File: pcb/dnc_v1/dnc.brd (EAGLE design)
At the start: 97.2 x 88 mm, 132 parts, among them IC1 LM2596S, IC2 74S244DW, Q1 IRF9321PBF, Q10 BSS316, Q11 BSS316, Q12 BSS138, Q13 BSS138, Q2 BSS670, Q3 BSS138, Q4 BSS670, Q5 BSS138, Q6 BSS670, Q7 BSS138, Q8 BSS138, Q9 BSS670, U1 MAX202CDWR, U2 74HCT595D, U3 TC7SU04F, U4 AL8807, U5 AL8807, U6 TC7SU04F

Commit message: BOM + carte insa
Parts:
- EXT1: value EXT1 -> EXT
- EXT2: value EXT2 -> EXT
- FLEX: value FLEX -> PLUG-3
- GYRO-LED: value GYRO LED -> PLUG-6
- IC2: value 74S244DW -> 74ACT244SC
- INPUT: value M08 -> PLUG-8
- L2, L3: value 100nH -> 100nH2.4A
- LED10W1: value LED10W1 -> PLUG-2
- LED10W2: value LED10W2 -> PLUG-2
- R12: value (none) -> 5.1K
- RELAY: value RELAY -> PLUG-3
- U4, U5: value AL8807 -> AL8805WS
- renumbered PLUG_3.81_1 to FLEX, PLUG_3.81_2 to RELAY, PLUG_3.81_2_1 to LED10W2, PLUG_3.81_2_2 to LED10W1, PLUG_3.81_6_1 to GYRO-LED, U$6 to INPUT

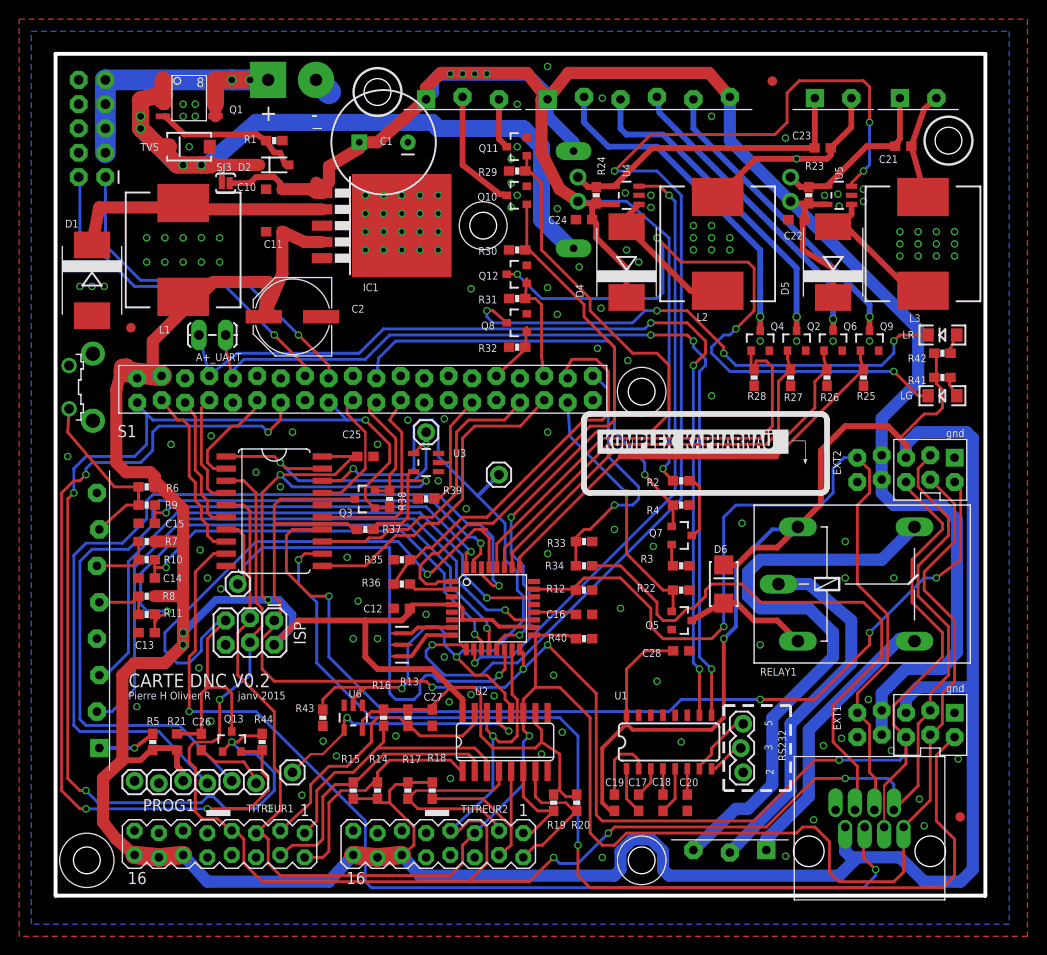
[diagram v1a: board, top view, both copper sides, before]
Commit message: minor debug (hole + value)
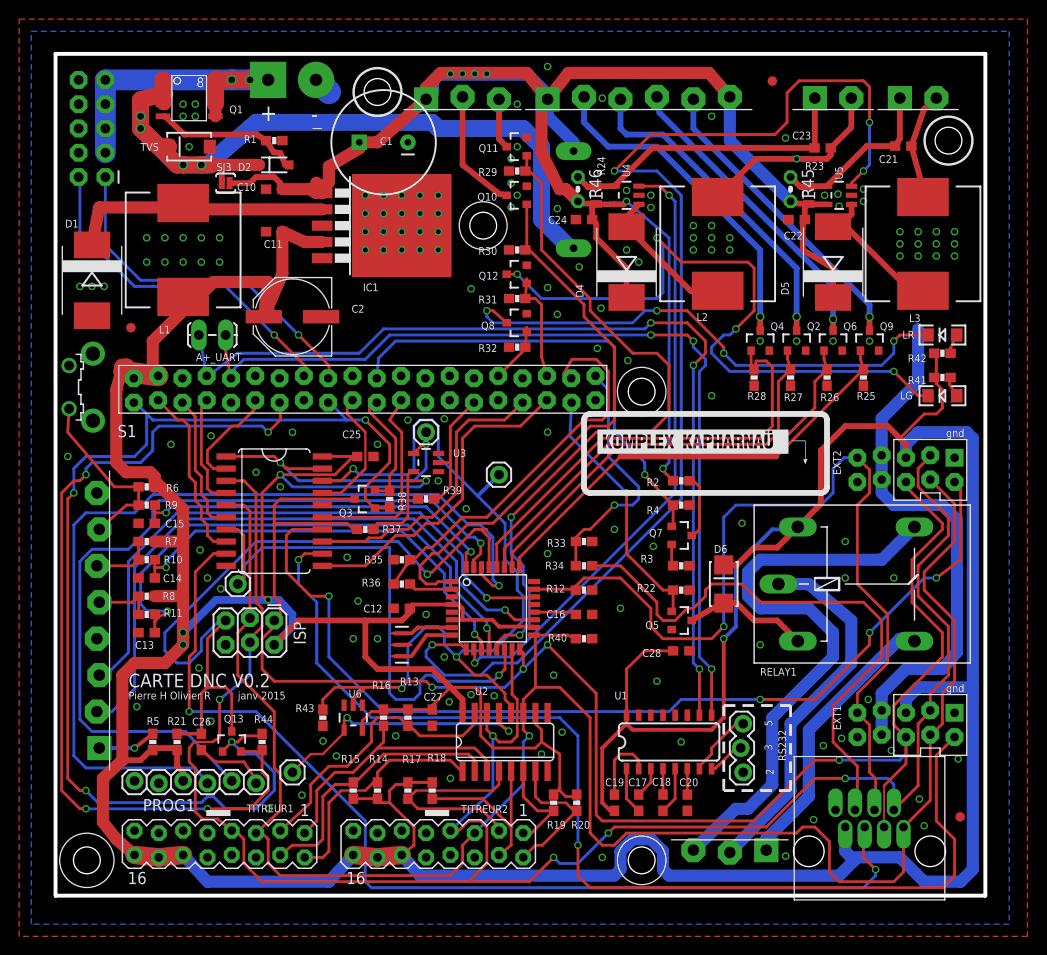
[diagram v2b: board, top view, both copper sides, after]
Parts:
- removed SJ1, SJ2: JUMPER-PTH-2-NO, SparkFun-Passives:PTH-JUMPER-2-NO_NO_SILK
- added R45, R46: OPTIONAL, rcl:0204V
- C1: value 680uF30mm -> 680uF
- R21: device rcl:R0603 -> SparkFun-Passives:0603-RES
- R23, R24: device SparkFun-Passives:0603-RES -> SparkFun-Passives:0805
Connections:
- net LED+1: now also R46.1; no longer SJ1.2
- net LED+2: now also R45.1; no longer SJ2.2
- net RAW_FUSED: now also R45.2, R46.2; no longer SJ1.1, SJ2.1
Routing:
- net RAW_FUSED: track 262.9 -> 240.4 mm, vias 5 -> 6
- net RX-I: track 92.2 -> 94.8 mm
- net +5V: track 568.4 -> 567.2 mm

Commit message: major change correction : - driver led position - add usb for power - correct max 202 voltage problem - titrer connector position - forget line - power trace consideration
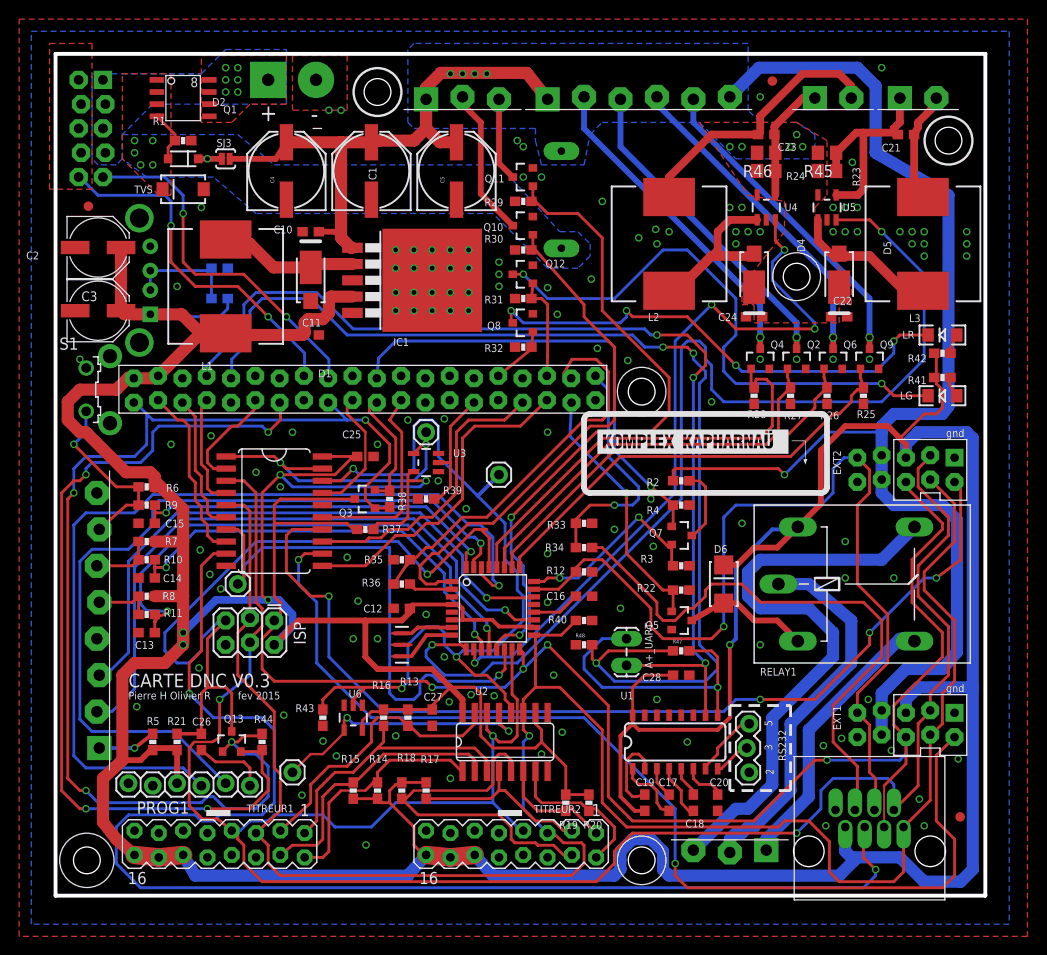
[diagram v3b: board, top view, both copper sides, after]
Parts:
- added C3: 100u, rcl:PANASONIC_D
- added C4, C5: 220uF, SparkFun:PANASONIC_E
- added R47: 10K, SparkFun-Passives:0603-RES
- added R48: 20K, SparkFun-Passives:0603-RES
- added R49: 22K, SparkFun-Passives:0603-RES
- added R50: 33K, SparkFun-Passives:0603-RES
- added X1: USB, pierre_vv:USB_F_SATISTRONIC
- C1: value 680uF -> 220uF; device SparkFun:CPOL-RADIAL-1000UF-25V -> SparkFun:PANASONIC_E
- C2: value 220u -> 100u; device rcl:PANASONIC_E -> rcl:PANASONIC_D
- D1, D4, D5: device diode:SMC -> pierre_vv:DO-221
- JP1: device SparkFun:2X5-SHROUDED_LOCK -> pierre_vv:2X5_LOCK
- R23, R24: device SparkFun-Passives:0805 -> rcl:R0805
- R45, R46: device rcl:0204V -> rcl:R0805
- moved A+_UART 56.3 mm to (59.7, 20.2), turned to 90 degrees
- moved U$1 33.2 mm to (77.5, 60.7), turned to 270 degrees
- moved D1 22.9 mm to (26.7, 60.3), turned to 90 degrees
- moved C2 21.6 mm to (4.45, 63.8), turned to 0 degrees
- moved C24 20.5 mm to (73.0, 56.5)
- moved R46 20.1 mm to (74.3, 73.7), turned to 180 degrees
- moved R24 18.0 mm to (74.3, 71.8), turned to 180 degrees
- moved U4 14.7 mm to (74.3, 67.9), turned to 0 degrees
- moved JP13 13.5 mm to (3.43, 68.1)
- moved D4 13.4 mm to (73.0, 61.0), turned to 270 degrees
- moved C11 11.4 mm to (26.7, 54.6), turned to 0 degrees
- moved C22 11.1 mm to (81.9, 56.5), turned to 0 degrees
- moved D2 9.55 mm to (13.3, 73.0), turned to 180 degrees
- moved R1 9.52 mm to (13.3, 74.9)
- moved TITREUR2 7.62 mm to (47.6, 1.40)
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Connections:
- net TXA+ renamed TXA+_5V
- removed net ANALOG_BAT: AT328.24
- new net N$26: R49.2, R50.2, X1.DM, X1.DP
- new net RXA+_5V: A+_UART.2, R47.2, U1.9
- net +5V: now also C3.+, R50.1, X1.+
- net ANALOG_RAW: now also AT328.24
- net GND: now also C1.-, C3.-, C4.-, C5.-, R48.1, R49.1, X1.-, X1.S1, X1.S2; no longer C1.2
- net RAW_FUSED: now also C1.+, C4.+, C5.+; no longer C1.1
- net RXA+: now also R47.1, R48.2; no longer A+_UART.2, U1.9
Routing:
- net RAW_POL_PROTECTED: track 86.7 -> 2.47 mm, vias 4 -> 6
- net RAW_FUSED: track 240.4 -> 195.8 mm, vias 6 -> 10
- net TELECO_CS_5V: track 108.2 -> 143.6 mm
- net RAW_UNPROTECTED: track 34.0 -> 0.00 mm, vias 2 -> 6
- net RXA+_5V: track 0.00 -> 30.6 mm, vias 0 -> 1
- net RXA+: track 96.0 -> 116.4 mm
- net LED+1: track 32.1 -> 12.7 mm
- net MOSI_5V: track 209.3 -> 228.5 mm, vias 5 -> 3
- net ANALOG_RAW: track 2.29 -> 20.9 mm, vias 0 -> 2
- net RST8: track 18.8 -> 37.2 mm
- net N$1: track 31.4 -> 14.6 mm
- net PWM_LED_1: track 124.0 -> 109.1 mm, vias 4 -> 2
- net +5V: track 567.2 -> 580.5 mm
- net PWM_LED_2: track 64.7 -> 77.1 mm, vias 2 -> 4
- net N$26: track 0.00 -> 11.7 mm
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- added copper zone on layer 1, net RAW_FUSED
- added copper zone on layer 16, net RAW_FUSED
- added copper zone on layer 1, net RAW_POL_PROTECTED
- added copper zone on layer 16, net RAW_POL_PROTECTED
- added copper zone on layer 1, net RAW_UNPROTECTED
- added copper zone on layer 16, net RAW_UNPROTECTED
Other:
- board text added: "BRD+4mm diam4mm"
- board text added: "CARTE DNC V0.3"
- board text added: "fev 2015"
- board text added: "titreur BRD+7mm"
- board text removed: "BRD+7,1mm diam4mm"
- board text removed: "CARTE DNC V0.2"
- board text removed: "janv 2015"

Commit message: fix text place and size
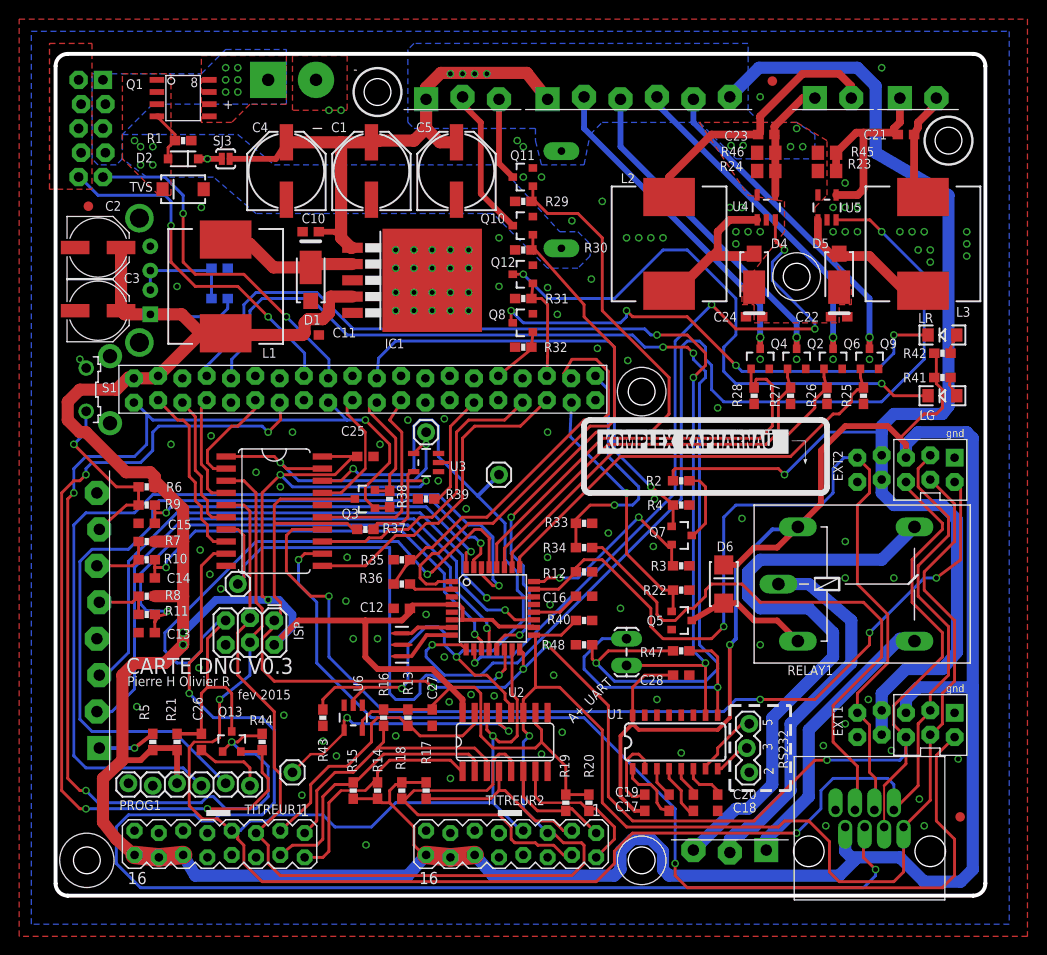
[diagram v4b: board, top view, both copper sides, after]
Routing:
- net RESET_5V: track 81.3 -> 80.7 mm
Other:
- outline, holes or cut-outs redrawn

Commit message: minor change : - logo size - add fuse on led - enclosure
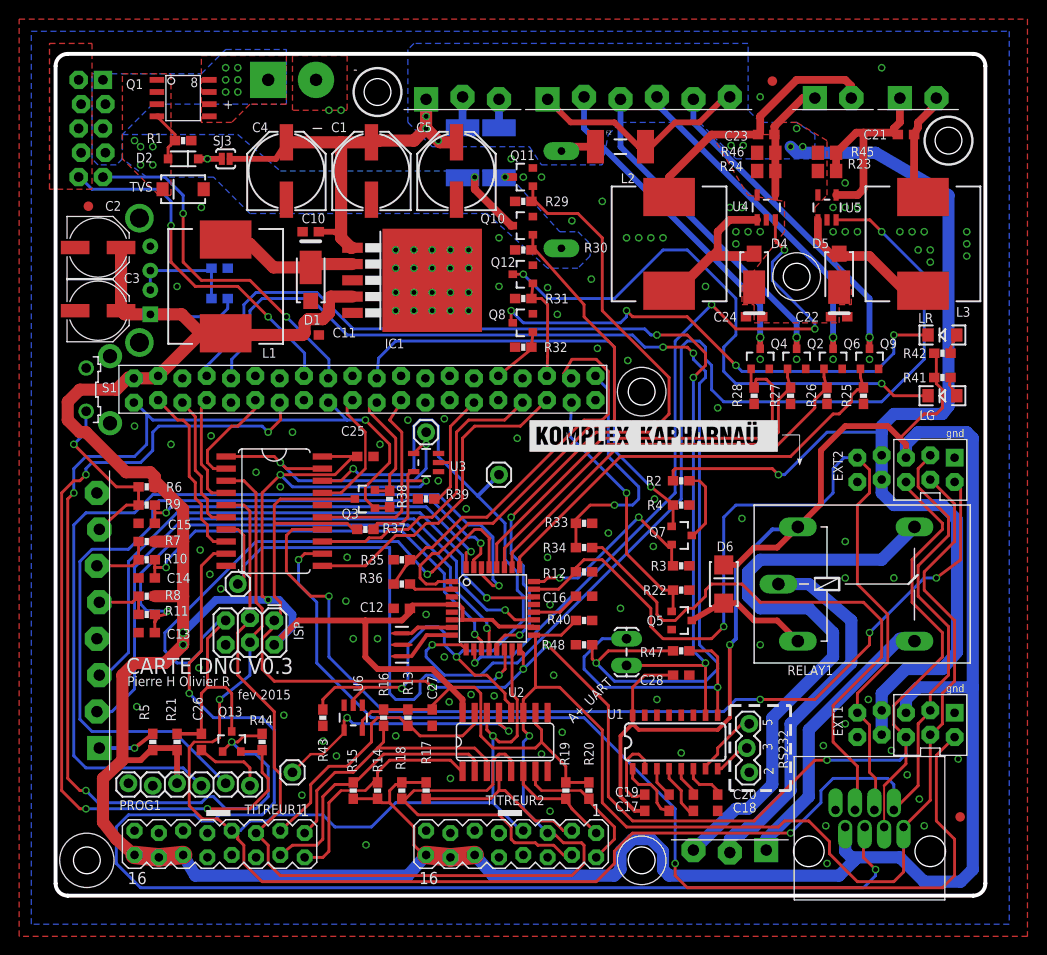
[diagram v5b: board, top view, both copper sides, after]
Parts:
- added F2, F3, F4: PTC1812, pierre_vv:PTC_1812
- U$2: value LOGO -> LOGOSIZE2; device pierre_vv:KXKMLOGO -> pierre_vv:KXKMLOGO2
- moved U$2 15.9 mm to (49.5, 38.7)
- moved R19 1.27 mm to (53.3, 6.99)
- moved R20 1.27 mm to (55.8, 6.99)
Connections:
- new net N$17: F4.1, Q11.3
- new net N$19: F3.1, Q10.3
- new net N$5: F2.2, GYRO-LED.1, GYRO-LED.6
- net N$14: now also F4.2, FLEX.3; no longer FLEX.2, Q10.3
- net N$9: now also F3.2, FLEX.2; no longer FLEX.3, Q11.3
- net RAW_FUSED: now also F2.1; no longer GYRO-LED.1, GYRO-LED.6
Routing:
- net RAW_FUSED: track 195.8 -> 163.7 mm, vias 10 -> 9
- net N$5: track 0.00 -> 23.3 mm
- net N$14: track 15.6 -> 2.97 mm
- net N$19: track 0.00 -> 8.13 mm, vias 0 -> 1
- net N$9: track 8.72 -> 3.23 mm
- net N$17: track 0.00 -> 1.47 mm, vias 0 -> 1
- net +5V: track 580.5 -> 579.2 mm
- net SCK_5V: track 212.9 -> 211.8 mm
- net RST6: track 16.4 -> 15.5 mm
- net RST5: track 12.0 -> 11.3 mm
- net LED-1: track 28.8 -> 28.3 mm

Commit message: change minor : - add rj45 for led string - add select pam led or flex
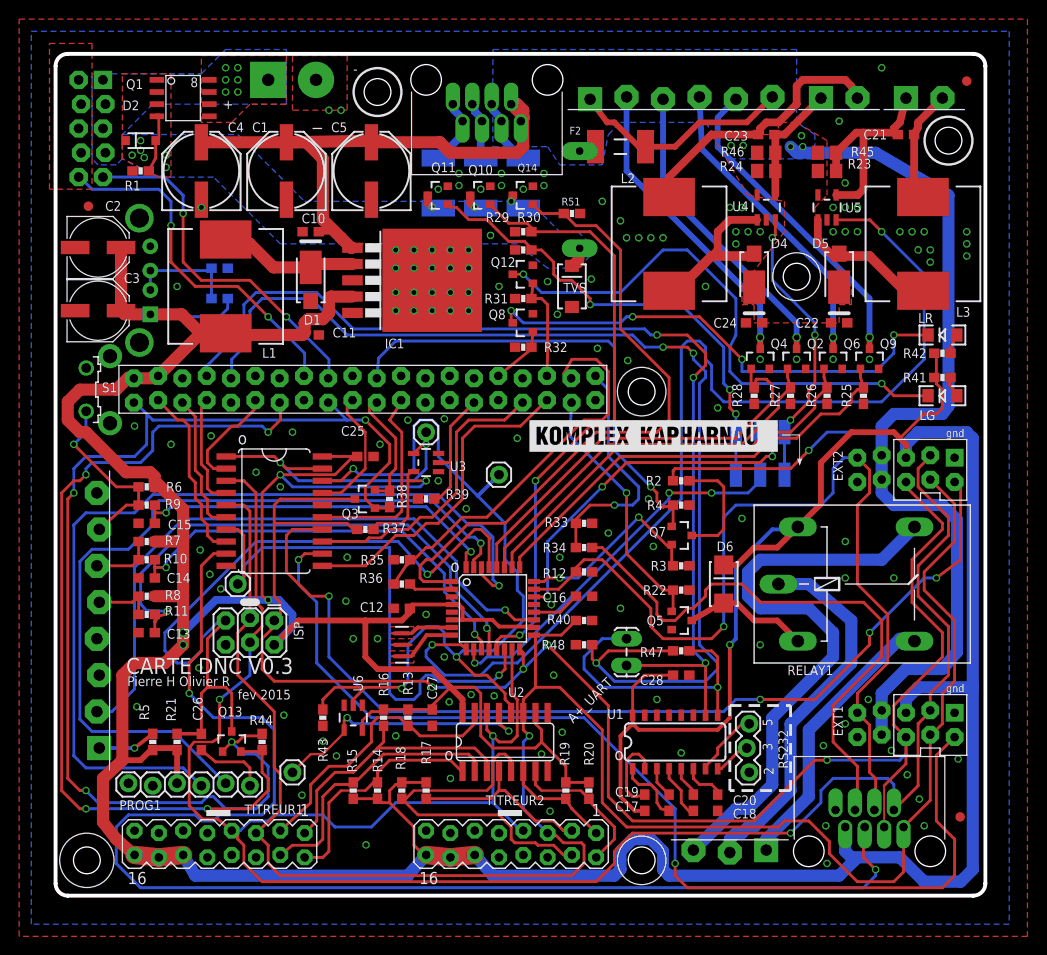
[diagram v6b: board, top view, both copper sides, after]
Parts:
- removed FLEX: PLUG-3, pierre_vv:PLUG_03
- removed SJ3: JUMPER-PAD-2-NC_BY_PASTE, SparkFun-Passives:PAD-JUMPER-2-NC_BY_PASTE_YES_SILK
- added F5: PTC1812, pierre_vv:PTC_1812
- added Q14: BSS316, SparkFun-DiscreteSemi:SOT23-3
- added R51: 100K, SparkFun-Passives:0603-RES
- added RGB-LED: RJ45-RGBLED, con-amphenol-rj45-ld:RJ45-TRAFO
- added SJ1, SJ2: JUMPER-PAD-3-NO, SparkFun-Passives:PAD-JUMPER-3-NO_YES_SILK_FULL_BOX_WIDE_SPACING
- R45, R46: value OPTIONAL -> OPT
- moved TVS 41.9 mm to (54.0, 59.7), turned to 90 degrees
- moved JP14 20.3 mm to (95.2, 81.2)
- moved Q11 9.09 mm to (40.0, 69.2)
- moved C1 8.89 mm to (24.1, 71.8)
- moved C4 8.89 mm to (15.2, 71.8)
- moved C5 8.89 mm to (33.0, 71.8)
- moved F4 7.10 mm to (40.0, 70.5)
- moved R1 5.46 mm to (8.89, 71.8), turned to 180 degrees
- moved Q10 5.46 mm to (44.5, 69.2)
- moved R29 5.08 mm to (48.9, 63.5)
- moved D2 4.84 mm to (8.89, 74.9), turned to 0 degrees
- moved GYRO-LED 4.45 mm to (65.4, 79.4)
- moved F3 3.70 mm to (44.5, 70.5)
- moved R30 1.91 mm to (48.9, 65.4)
- moved F1 1.90 mm to (54.8, 68.8)
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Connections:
- removed net FLOAT2: AT328.22, INPUT.3
- new net DIGITAL_LED2_OR_FLEX3: AT328.22, SJ1.2
- new net N$29: F5.2, RGB-LED.3, RGB-LED.4
- new net N$30: F5.1, Q14.3
- new net PWM_FLEX_3: Q11.1, R29.2, SJ1.3, SJ2.3
- new net PWM_LED2_OR_FLEX3: AT328.10, SJ2.2
- net GND: now also Q14.2, R51.1
- net N$14: now also RGB-LED.7, RGB-LED.8; no longer FLEX.3
- net N$9: now also RGB-LED.5, RGB-LED.6; no longer FLEX.2
- net PWM_FLEX_1: now also Q14.1, R51.2; no longer Q10.1, R30.2
- net PWM_FLEX_2: now also Q10.1, R30.2; no longer Q11.1, R29.2
- net PWM_LED_2: now also SJ1.1, SJ2.1; no longer AT328.10
- net RAW_FUSED: now also RGB-LED.1, RGB-LED.2; no longer FLEX.1, SJ3.2
- net RAW_POL_PROTECTED: no longer SJ3.1
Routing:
- net FLOAT2: track 63.0 -> 0.00 mm, vias 1 -> 0
- net PWM_FLEX_3: track 0.00 -> 50.1 mm, vias 0 -> 3
- net PWM_LED_2: track 77.1 -> 29.9 mm, vias 4 -> 3
- net PWM_LED2_OR_FLEX3: track 0.00 -> 40.2 mm, vias 0 -> 3
- net DIGITAL_LED2_OR_FLEX3: track 0.00 -> 37.4 mm, vias 0 -> 3
- net RAW_FUSED: track 163.7 -> 179.9 mm, vias 9 -> 6
- net PWM_FLEX_1: track 54.7 -> 68.1 mm
- net N$29: track 0.00 -> 7.13 mm
- net N$19: track 8.13 -> 2.13 mm
- net PWM_FLEX_2: track 69.9 -> 63.9 mm
- net N$14: track 2.97 -> 7.16 mm
- net N$3: track 7.73 -> 11.9 mm
- net N$9: track 3.23 -> 6.11 mm
- net N$30: track 0.00 -> 2.23 mm, vias 0 -> 1
- net N$12: track 33.9 -> 32.0 mm
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- added copper zone on layer 1, net N$27
- added copper zone on layer 1, net N$28
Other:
- board text added: "DIGITAL"
- board text added: "FLEX B"
- board text added: "LED 10W 2"
- board text added: "PWM"
- board text added: "o"
